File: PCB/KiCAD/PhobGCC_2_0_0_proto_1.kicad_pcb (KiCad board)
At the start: 2 copper layers, 125.5 x 90.3 mm, 113 parts, among them J1 Conn_01x06_Female, J11 Conn_01x02, J14 Conn_01x06, J15 Conn_01x06, J2 Conn_01x02, J3 Conn_01x02, J4 Conn_01x01, J5 Rumble, J6 Conn_01x06, J8 USB_B_Micro, Q1 Q_NMOS_GSD, Q2 Q_PMOS_GDS, Q3 Q_NMOS_GSD, SW1 A, SW10 Dup, SW11 Dright, SW12 Ddown, SW2 B, SW3 X, SW4 Y, SW5 Start, SW6 L, SW7 R, SW8 Z, SW9 Dleft, U1 MCP3202, U10 DRV5055A3xDBZxQ1, U11 DRV5055A3xDBZxQ1, U12 USBLC6-2P6, U13 USBLC6-2P6, U2 Stickbox_Assembly_Main, U3 MCP3202, U4 DRV5055A3xDBZxQ1, U5 Stickbox_Assembly_CStick, U6 AMS1117-3.3, U7 W25Q128JVS, U8 RP2040, U9 DRV5055A3xDBZxQ1, Y1 Crystal_GND24

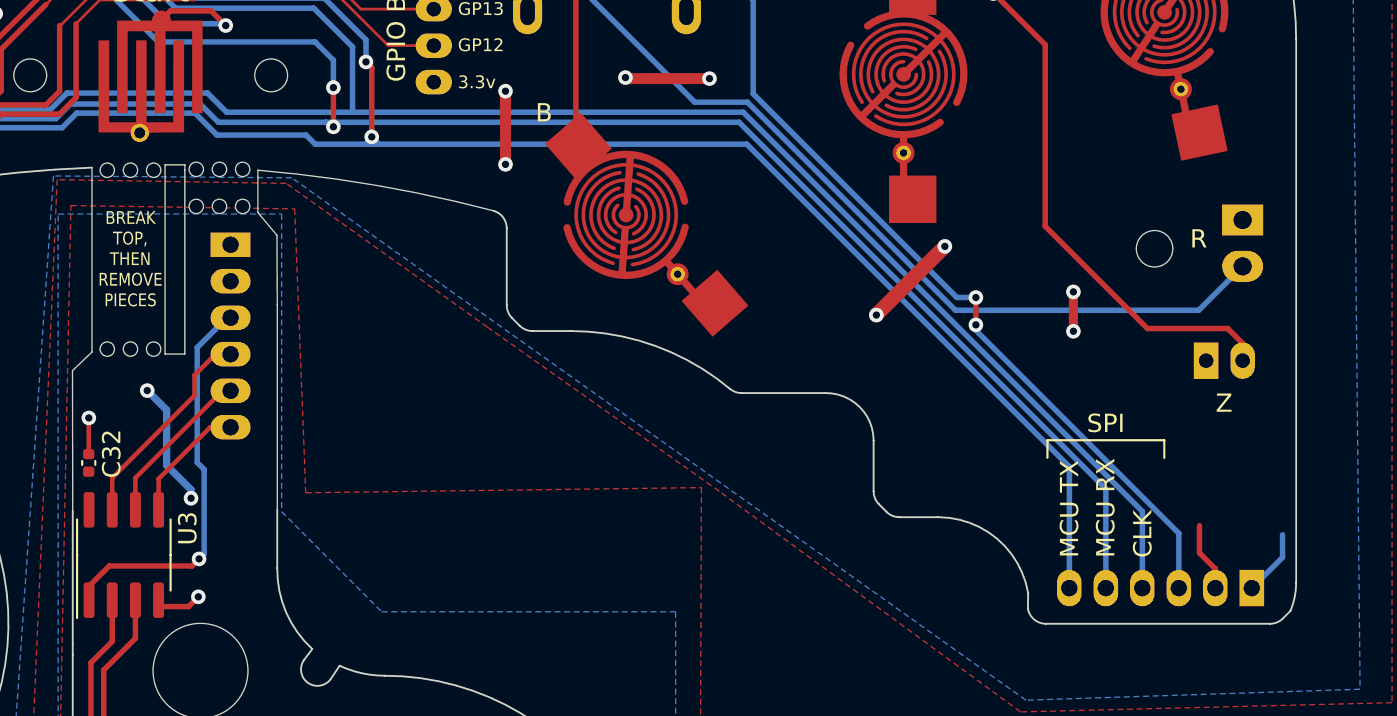
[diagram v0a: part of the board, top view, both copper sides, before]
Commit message: Changes location of C-stick header Changes C-stick header pitch to 2.54 mm (100 mil)
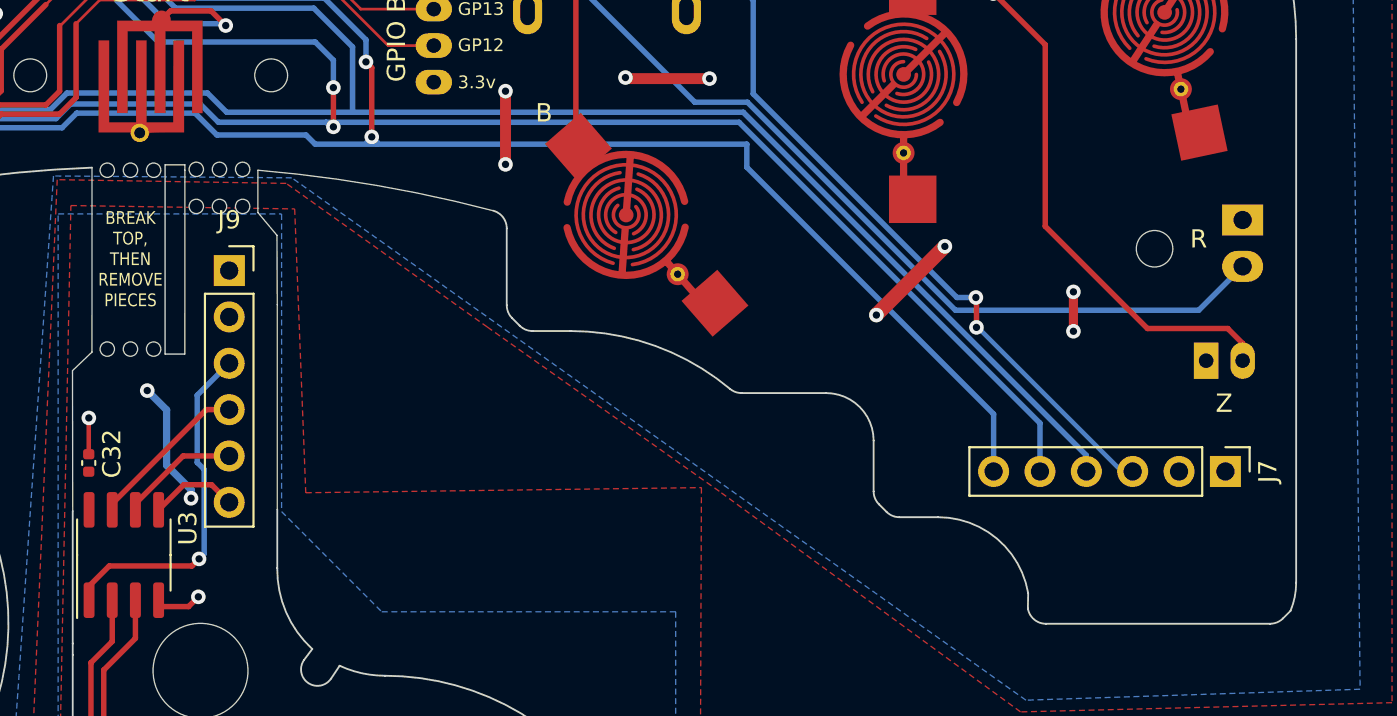
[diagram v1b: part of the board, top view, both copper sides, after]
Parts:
- removed J14, J15: Conn_01x06, PhobGCC_2_0_0_footprints:PinSocket_1x06_P2.00mm_Vertical
- added J7: Conn_01x06, Connector_PinHeader_2.54mm:PinHeader_1x06_P2.54mm_Vertical, F.Cu at (169.9, 72.8)
- added J9: Conn_01x06, Connector_PinSocket_2.54mm:PinSocket_1x06_P2.54mm_Vertical, F.Cu at (115.3, 61.8)
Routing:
- net /Din: track 125.5 -> 117.5 mm
- net /Dout: track 127.9 -> 120.1 mm
- net /CLK: track 128.3 -> 120.7 mm
- net /CS2: track 94.4 -> 88.0 mm
- net +3V3: track 66.6 -> 62.8 mm
- net GND: track 140.9 -> 137.3 mm
- net /CLK2: track 11.7 -> 8.88 mm
- net /CS2_2: track 22.1 -> 19.5 mm
- net /Dout2: track 8.94 -> 6.56 mm
- net /Din2: track 6.81 -> 4.84 mm
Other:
- board text removed: "CLK"
- board text removed: "MCU RX"
- board text removed: "MCU TX"
- board text removed: "SPI"

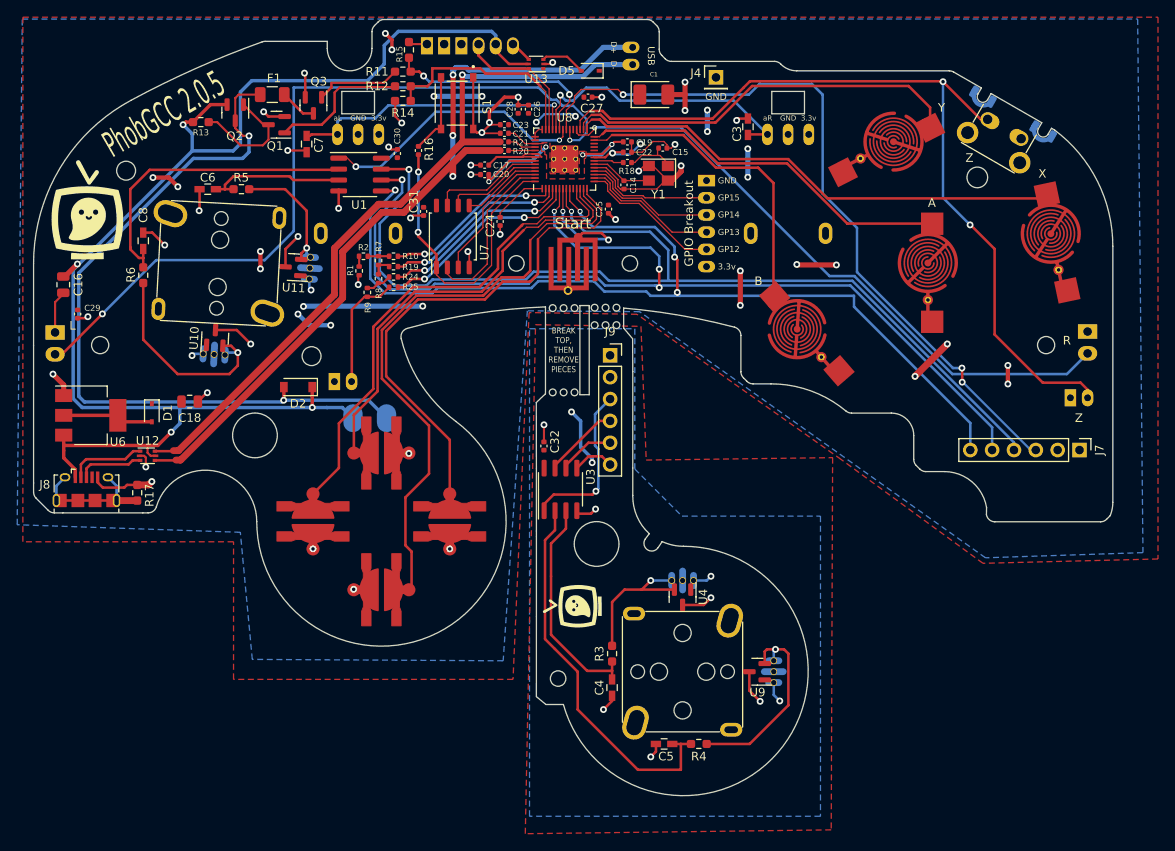
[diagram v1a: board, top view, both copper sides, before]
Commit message: Updates repo name on board and adds 'Backward Aerial Bros.'
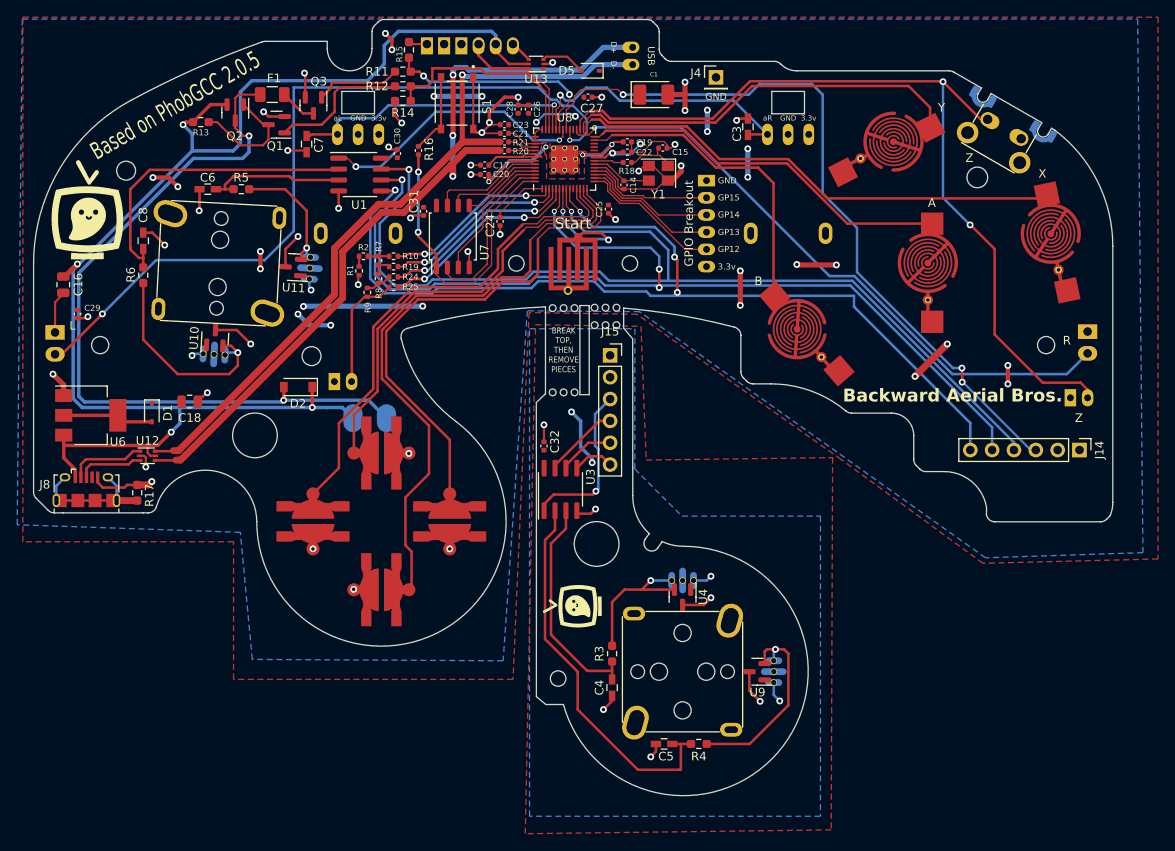
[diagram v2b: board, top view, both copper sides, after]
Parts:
- renumbered J7 to J14, J9 to J15
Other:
- board text added: "Backward Aerial Bros."
- board text added: "Based on PhobGCC 2.0.5"
- board text added: "https://github.com/tommybair/PhobGCCv2-HW"
- board text removed: "PhobGCC 2.0.5"
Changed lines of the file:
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@@
     (property "ki_keywords" "connector")
     (attr through_hole)
-    (fp_text reference "J7" (at 0 -2.33 90) (layer "F.SilkS")
+    (fp_text reference "J14" (at 0 -2.33 90) (layer "F.SilkS")
         (effects (font (size 1 1) (thickness 0.15)))
     )
@@
     (property "ki_keywords" "connector")
     (attr through_hole)
-    (fp_text reference "J9" (at 0 -2.77) (layer "F.SilkS")
+    (fp_text reference "J15" (at 0 -2.77) (layer "F.SilkS")
         (effects (font (size 1 1) (thickness 0.15)))
     )
@@
     (effects (font (size 0.7 0.7) (thickness 0.15)) (justify left mirror))
   )
-  (gr_text "github.com/PhobGCC" (at 157.734 49.8856) (layer "B.SilkS")
-    (effects (font (size 1.5 1.5) (thickness 0.35)) (justify mirror))
+  (gr_text "https://github.com/tommybair/PhobGCCv2-HW" (at 145.99 54.98) (layer "B.SilkS")
+    (effects (font (size 1.5 1.5) (thickness 0.35) bold) (justify mirror))
   )
   (gr_text "github.com/PhobGCC" (at 112.6352 66.9968 90) (layer "B.SilkS")
@@
     (effects (font (size 0.65 0.65) (thickness 0.15)) (justify mirror))
   )
-  (gr_text "Licensed under" (at 157.734 43.4848) (layer "B.SilkS")
+  (gr_text "Licensed under" (at 157.67 46.66) (layer "B.SilkS")
     (effects (font (size 1 1) (thickness 0.15)) (justify mirror))
   )
@@
     (effects (font (size 0.7 0.7) (thickness 0.15)) (justify left mirror))
   )
-  (gr_text "CERN-OHL-S v2" (at 157.734 45.3136) (layer "B.SilkS")
+  (gr_text "CERN-OHL-S v2" (at 157.75 49.38) (layer "B.SilkS")
     (effects (font (size 1.5 1.5) (thickness 0.35)) (justify mirror))
   )
@@
     (effects (font (size 0.7 0.7) (thickness 0.15)) (justify right mirror))
   )
-  (gr_text "Source files" (at 157.734 48.0568) (layer "B.SilkS")
+  (gr_text "Source files" (at 157.83 52.1) (layer "B.SilkS")
     (effects (font (size 1 1) (thickness 0.15)) (justify mirror))
   )
@@
     (effects (font (size 0.6 0.6) (thickness 0.1)))
   )
-  (gr_text "PhobGCC 2.0.5" (at 63.4 33.782 30) (layer "F.SilkS")
-    (effects (font (size 3 1.5) (thickness 0.3)))
+  (gr_text "Based on PhobGCC 2.0.5" (at 64.73 32.76 30) (layer "F.SilkS")
+    (effects (font (size 2 1.3) (thickness 0.3)))
   )
   (gr_text "aR" (at 133.604 34.2392) (layer "F.SilkS")
@@
     (effects (font (size 0.6 0.6) (thickness 0.1)))
   )
+  (gr_text "Backward Aerial Bros." (at 142.34 67.37) (layer "F.SilkS")
+    (effects (font (size 1.5 1.5) (thickness 0.3) bold) (justify left bottom))
+  )
   (gr_text "3.3v" (at 88.392 34.2392) (layer "F.SilkS")
